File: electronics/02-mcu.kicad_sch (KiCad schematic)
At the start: 30 parts, among them J201 TC2050-IDC-NL, U201 STM32H723VGT6, Y201 25 MHz / 10 ppm

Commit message: Passe le microcontrôleur en LQFP144 et lit les deux courants au même instant
Le LQFP100 avait ses seize entrées ADC prises — douze voies de ligne, trois
de télémétrie, une sortie de multiplexeur — et c'est ce multiplexeur qui
posait le vrai problème : il interdisait par construction de lire les deux
courants moteur ensemble. On lisait un moteur, on commutait, on attendait
l'établissement, on lisait l'autre. Le STM32H723ZGT6 en LQFP144 place
PF11 sur ADC1_INP2 et PF13 sur ADC2_INP2 : même numéro de voie sur deux
convertisseurs, donc une lecture simultanée en mode double, et le 74HC4051
disparaît de la carte.

Le brochage étant donné par nom de port et non par numéro de broche, le
passage a coûté deux affectations sur quatre-vingt-sept. Une affectation est
un choix de port — PA0 porte la voie de ligne 00 — jamais un choix de patte.
Une table numérotée aurait demandé de recopier 144 lignes à la main, et une
erreur de brochage ne se voit pas à l'ERC.

Ajoute une huitième feuille, les témoins de ligne. Ce qu'on regarde pendant
un essai n'est pas un témoin d'état générique, c'est ce que voit la
moustache : une LED par capteur, à l'aplomb du capteur qu'elle rapporte, et
un capteur borgne se voit avant la course plutôt qu'après. Le rapport
cyclique suit le signal, sinon rien ne dirait si la ligne est au bord ou au
centre du trait. PCA9685 à l'adresse 0x40 sur I²C2, 52 octets par rafale
soit 1,2 ms à 400 kHz, en DMA hors de la boucle rapide.

Remplace l'interrupteur à glissière par une mise sous tension à bouton
poussoir : une impulsion amorce, le microcontrôleur se tient lui-même, et
c'est lui qui coupe. La glissière demandait une place au bord de carte que
le pack, l'équilibrage et les fils de l'ESC ont fini par prendre — et elle
ne savait pas éteindre proprement, couper le 3,3 V sous les pieds du
firmware n'ayant jamais rien écrit dans la flash.

Ajoute au générateur le contrôle qui manquait : deux extrémités de nets
différents au même point. Il a fallu qu'il relie B+ à B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
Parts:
- removed TP201: BOOT0, TestPoint:TestPoint_Pad_D1.5mm, symbol Connector:TestPoint
- removed TP202: TP_PE4, TestPoint:TestPoint_Pad_D1.5mm, symbol Connector:TestPoint
- removed TP203: TP_PE5, TestPoint:TestPoint_Pad_D1.5mm, symbol Connector:TestPoint
- removed TP204: TP_PA15, TestPoint:TestPoint_Pad_D1.5mm, symbol Connector:TestPoint
- removed TP205: TP_PC13, TestPoint:TestPoint_Pad_D1.5mm, symbol Connector:TestPoint
- removed TP206: TP_PC14, TestPoint:TestPoint_Pad_D1.5mm, symbol Connector:TestPoint
- removed TP207: TP_PC15, TestPoint:TestPoint_Pad_D1.5mm, symbol Connector:TestPoint
- added C217, C218, C219, C220, C221, C222: 100nF, Capacitor_SMD:C_0402_1005Metric, symbol Device:C
- added SW603: RESET, Button_Switch_SMD:SW_SPST_B3U-1000P, symbol Switch:SW_Push
- C201, C202, C203, C204, C205, C207, C208, C210, C214: footprint Capacitor_SMD:C_0603_1608Metric -> Capacitor_SMD:C_0402_1005Metric; Dielectric (none) -> X7R; Voltage (none) -> 25V
- C206: value 4u7F/10V -> 4u7F; Dielectric (none) -> X5R; Voltage (none) -> 10V
- C209, C211: footprint Capacitor_SMD:C_0603_1608Metric -> Capacitor_SMD:C_0402_1005Metric; Dielectric (none) -> X5R; Voltage (none) -> 16V
- C212, C213: value 2u2F/10V -> 2u2F; Dielectric (none) -> X5R; Voltage (none) -> 10V
- C215, C216: footprint Capacitor_SMD:C_0603_1608Metric -> Capacitor_SMD:C_0402_1005Metric; Dielectric (none) -> C0G; Voltage (none) -> 50V
- J201: value TC2050-IDC-NL -> TC2030-IDC-FP; footprint Connector:Tag-Connect_TC2050-IDC-NL_2x05_P1.27mm_Vertical -> Connector:Tag-Connect_TC2030-IDC-FP_2x03_P1.27mm_Vertical; symbol Connector:TC2050 -> Connector:TC2030
- R201, R202, R203, R204: footprint Resistor_SMD:R_0603_1608Metric -> Resistor_SMD:R_0402_1005Metric; Power (none) -> 63mW
- U201: value STM32H723VGT6 -> STM32H723ZGT6; footprint Package_QFP:LQFP-100_14x14mm_P0.5mm -> Package_QFP:LQFP-144_20x20mm_P0.5mm; symbol MCU_ST_STM32H7:STM32H723VGTx -> MCU_ST_STM32H7:STM32H723ZGTx; LCSC C730142 -> C730146
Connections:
- net IR_LASER_EN is gone; now on net LINE_02: U201.36 (PA2)
- net LED_ERROR is gone; now on net SW_DOWN: U201.65 (PE12)
- net LED_STATUS is gone; now on net +3V3: U201.62 (VDD)
- net LED_USER is gone; now on net MOT_R_IN1: U201.66 (PE13)
- net TOF_F_INT is gone; now on net ENC_R_B: U201.97 (PC7)
- net TP_PE4 is gone; now on net CHG_INT: U201.3 (PE4)
- net +3V3: now also U201.108 (VDD), U201.121 (VDD), U201.131 (VDD), U201.143 (PDR_ON), U201.144 (VDD), U201.17 (VDD), U201.30 (VDD), U201.39 (VDD), U201.52 (VDD), U201.72 (VDD), U201.84 (VDD), U201.95 (VDD33USB), C217.1, C218.1, C219.1, C220.1, C221.1, C222.1; no longer U201.100 (VDD), U201.11 (VDD), U201.27 (VDD), U201.50 (VDD), U201.75 (VDD)
- net +3V3A: now also U201.32 (VREF+), U201.33 (VDDA); no longer U201.20 (VREF+), U201.21 (VDDA)
- net BLE_PWR_EN: now also U201.100 (PA8); no longer U201.67 (PA8)
- net BLE_RX: now also U201.102 (PA10); no longer U201.69 (PA10)
- net BLE_TX: now also U201.101 (PA9); no longer U201.68 (PA9)
- net BOOT0: now also U201.138 (BOOT0); no longer U201.94 (BOOT0)
- net BUZZER: now also U201.140 (PB9); no longer U201.96 (PB9)
- net CHG_CD_EN: now also U201.2 (PE3); no longer U201.1 (PE2)
- net CHG_INT: no longer U201.2 (PE3)
- net ENC_L_A: now also U201.134 (PB4(NJTRST)); no longer U201.90 (PB4(NJTRST))
- net ENC_L_B: now also U201.135 (PB5); no longer U201.91 (PB5)
- net ENC_R_A: now also U201.96 (PC6); no longer U201.63 (PC6)
- net ENC_R_B: no longer U201.64 (PC7)
- net ESC_PWM: now also U201.139 (PB8); no longer U201.95 (PB8)
- net FLASH_MISO: now also U201.112 (PC11); no longer U201.79 (PC11)
- net FLASH_MOSI: now also U201.113 (PC12); no longer U201.80 (PC12)
- net FLASH_SCK: now also U201.111 (PC10); no longer U201.78 (PC10)
- net FLASH_nCS: now also U201.116 (PD2); no longer U201.83 (PD2)
- net GND: now also J201.6, U201.107 (VSS), U201.120 (VSS), U201.130 (VSS), U201.16 (VSS), U201.31 (VSSA), U201.38 (VSS), U201.51 (VSS), U201.61 (VSS), U201.83 (VSS), U201.94 (VSS), C217.2, C218.2, C219.2, C220.2, C221.2, C222.2, SW603.2; no longer J201.3, J201.5, J201.9, U201.10 (VSS), U201.19 (VSSA), U201.26 (VSS), U201.49 (VSS), U201.74 (VSS), U201.99 (VSS)
- net IMU_MISO: now also U201.75 (PB14); no longer U201.53 (PB14)
- net IMU_MOSI: now also U201.76 (PB15); no longer U201.54 (PB15)
- net IMU_SCK: now also U201.74 (PB13); no longer U201.52 (PB13)
- net IMU_nCS: now also U201.73 (PB12); no longer U201.51 (PB12)
- net IPROPI_L: now also U201.49 (PF11); no longer U201.16 (PC1)
- net IPROPI_R: now also U201.53 (PF13); no longer U201.17 (PC2_C)
- net IR_BANK_A: now also U201.58 (PE7); no longer U201.37 (PE7)
- net IR_BANK_B: now also U201.59 (PE8); no longer U201.38 (PE8)
- net LINE_00: now also U201.34 (PA0); no longer U201.22 (PA0)
- net LINE_01: now also U201.35 (PA1); no longer U201.23 (PA1)
- net LINE_02: no longer U201.24 (PA2)
- net LINE_03: now also U201.37 (PA3); no longer U201.25 (PA3)
- net LINE_04: now also U201.40 (PA4); no longer U201.28 (PA4)
- net LINE_05: now also U201.41 (PA5); no longer U201.29 (PA5)
- net LINE_06: now also U201.42 (PA6); no longer U201.30 (PA6)
- net LINE_07: now also U201.43 (PA7); no longer U201.31 (PA7)
- net LINE_08: now also U201.46 (PB0); no longer U201.34 (PB0)
- net LINE_09: now also U201.47 (PB1); no longer U201.35 (PB1)
- net LINE_10: now also U201.44 (PC4); no longer U201.32 (PC4)
- net LINE_11: now also U201.45 (PC5); no longer U201.33 (PC5)
- net MOT_L_IN1: now also U201.60 (PE9); no longer U201.39 (PE9)
- net MOT_L_IN2: now also U201.64 (PE11); no longer U201.41 (PE11)
- net MOT_L_nFAULT: now also U201.117 (PD3); no longer U201.84 (PD3)
- net MOT_L_nSLEEP: now also U201.114 (PD0); no longer U201.81 (PD0)
- net MOT_R_IN1: no longer U201.43 (PE13)
- net MOT_R_IN2: now also U201.67 (PE14); no longer U201.44 (PE14)
- net MOT_R_nFAULT: now also U201.118 (PD4); no longer U201.85 (PD4)
- net MOT_R_nSLEEP: now also U201.115 (PD1); no longer U201.82 (PD1)
- net NRST: now also J201.3, U201.25 (NRST), SW603.1; no longer J201.10, U201.14 (NRST)
- net OSC_IN: now also U201.23 (PH0); no longer U201.12 (PH0)
- net OSC_OUT: now also U201.24 (PH1); no longer U201.13 (PH1)
- net SCL2: now also U201.69 (PB10); no longer U201.46 (PB10)
- net SDA2: now also U201.70 (PB11); no longer U201.47 (PB11)
- net START_BTN: now also U201.85 (PD14); no longer U201.61 (PD14)
- net SWCLK: now also U201.109 (PA14(JTCK); no longer U201.76 (PA14(JTCK)
- net SWDIO: now also J201.5, U201.105 (PA13(JTMS); no longer J201.2, U201.72 (PA13(JTMS)
- net SWO: now also J201.2, U201.133 (PB3(JTDO); no longer J201.6, U201.89 (PB3(JTDO)
- net SW_DOWN: no longer U201.42 (PE12)
- net SW_LEFT: now also U201.68 (PE15); no longer U201.45 (PE15)
- net SW_PUSH: now also U201.82 (PD13); no longer U201.60 (PD13)
- net SW_RIGHT: now also U201.79 (PD10); no longer U201.57 (PD10)
- net SW_UP: now also U201.63 (PE10); no longer U201.40 (PE10)
- net USB_DM: now also U201.103 (PA11); no longer U201.70 (PA11)
- net USB_DP: now also U201.104 (PA12); no longer U201.71 (PA12)
- net VBAT_SENSE: now also U201.26 (PC0); no longer U201.15 (PC0)
- net VCAP1: now also U201.71 (VCAP); no longer U201.48 (VCAP)
- net VCAP2: now also U201.106 (VCAP); no longer U201.73 (VCAP)
- net SCL1: no longer names the net of U201.92 (PG7)
- net SDA1: no longer names the net of U201.93 (PG8)
- net TOF_ANA: no longer names the net of U201.18 (PF6)
- net TOF_FL_INT: no longer names the net of U201.98 (PC8)
- net TOF_FL_XSHUT: no longer names the net of U201.87 (PG2)
- net TOF_F_XSHUT: no longer names the net of U201.86 (PD15)
- net TP_PA15: no longer names the net of U201.77 (PD8)
- net TP_PC13 renamed TX_L
- net TP_PC14: no longer names the net of U201.8 (PC14)
- net TP_PC15: no longer names the net of U201.9 (PC15)
- net TP_PE5 renamed TRACK_EN
- new net PWR_BTN: U201.142 (PE1)
- new net PWR_HOLD: U201.141 (PE0)
- new net RX_F: U201.27 (PC1)
- new net RX_FL: U201.28 (PC2_C)
- new net RX_L: U201.29 (PC3_C)
- new net TX_F: U201.48 (PB2)
- new net TX_FL: U201.1 (PE2)
- no-connect marks 7 -> 45
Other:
- note added: "Bilan : 80 broches affectees, 45 libres et marquees non connectees au schema. Le LQFP144 apporte les ports F et G, soit 32 E/S de plus et surtout DOUZE entrees ADC supplementaires (PF3 a PF14) : c est ce qui a permis de supprimer le multiplexeur 74HC4051 et de lire les deux courants moteur au meme instant."
- note added: "C208/C209 : VDDA. C210/C211 : VREF+. C222 : VDD33USB, broche separee sur le LQFP144 alors que le LQFP100 la reliait en interne. VCAP : 2,2 uF ceramique, ESR < 2 ohm, tres pres du boitier. PDR_ON est tiree a VDD : reset interne d alimentation actif."
- note added: "Debogage SWD + SWO - Tag-Connect TC2030 (brochage Sp3ctra V4)"
- note added: "Decouplage - un 100 nF par broche VDD (elles sont onze)"
- note added: "Rails analogiques, USB et VCAP"
- note removed: "Bilan : 74 broches affectees sur 82 disponibles."
- note removed: "C208/C209 : VDDA C210/C211 : VREF+"
- note removed: "Debogage SWD + SWO - Tag-Connect TC2050-IDC-NL"
- note removed: "Decouplage - un 100 nF par broche VDD, au plus pres du boitier"
- note removed: "PD7-PD9 et PD11-PD12 restent libres, marques non connectes au schema."
- note removed: "Reserves sorties sur pastilles"
- note removed: "VCAP : 2,2 uF ceramique, ESR < 2 ohm, tres pres du boitier."
- title: UsainBot - STM32H723VGT6, horloge et debogage -> UsainBot - STM32H723ZGT6, horloge et debogage
- moved on the sheet: C201, C202, C203, C204, C205, C206, C207, C208, C209, C210, C211, C212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
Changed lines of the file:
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@@
 	(paper "A3")
 	(title_block
-		(title "UsainBot - STM32H723VGT6, horloge et debogage")
+		(title "UsainBot - STM32H723ZGT6, horloge et debogage")
 		(date "2026-08-30")
 		(rev "A")
 		(company "Pacabot")
-		(comment 1 "Mode LDO seul (AN5312) : le LQFP100 n expose pas les broches SMPS")
-		(comment 2 "PB3 est reserve au SWO, d ou l abandon de TIM2")
+		(comment 1 "Mode LDO seul (AN5312) : le LQFP144 n expose pas les broches SMPS")
+		(comment 2 "Passe du LQFP100 au LQFP144 le 4 septembre : 12 entrees ADC de plus")
 	)

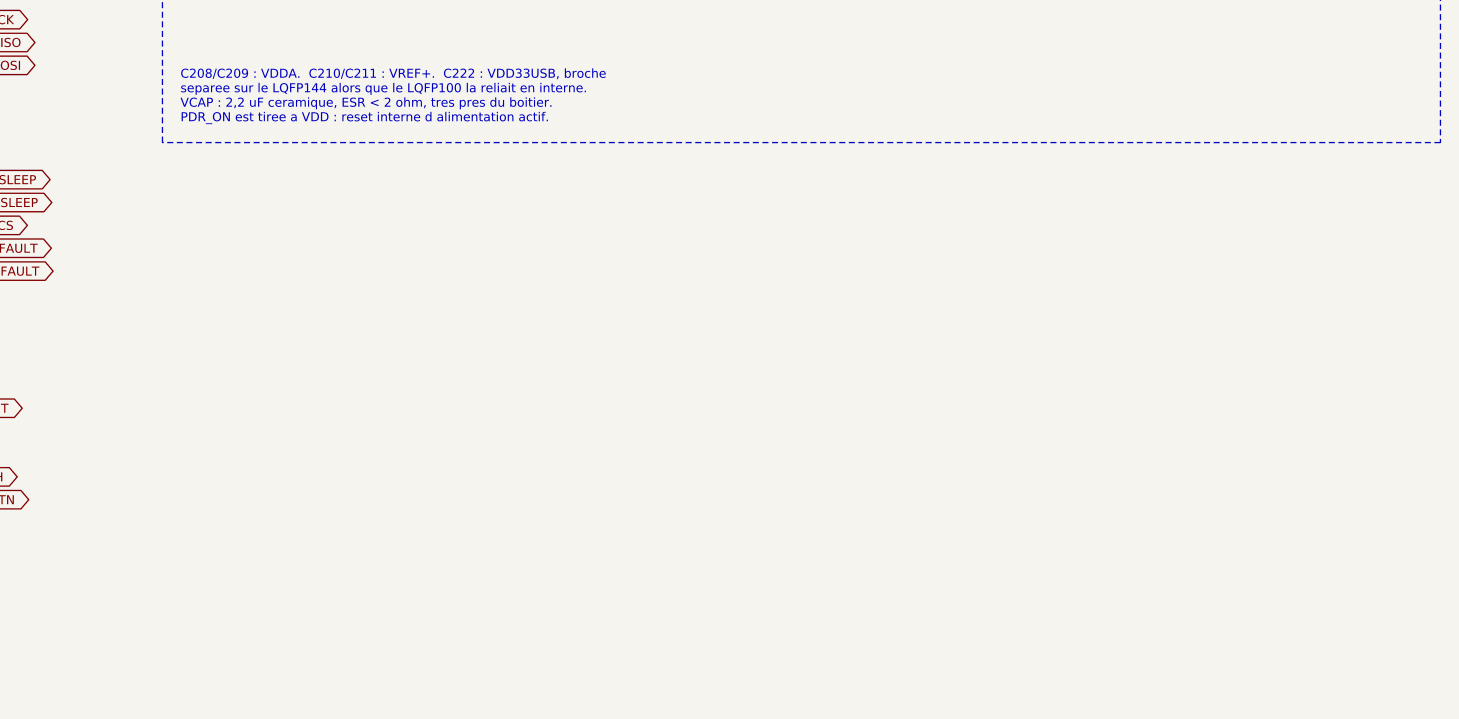
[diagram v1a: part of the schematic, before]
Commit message: Replace la carte autour de ses chaînes analogiques et y intègre le pack commun et l'ESC
Le placement du 4 septembre rangeait les pièces par zone. Celui-ci part des
nets et des vraies pastilles, et affecte chaque condensateur à une broche
plutôt qu'à une couronne autour du boîtier. Le STM32 pivote de 180° sur son
centre pour tourner son côté analogique vers la barrette. Chaque station
laser reçoit son propre TLV9064 (U504 s'ajoute pour la station L), et la
liaison photodiode → TIA tombe de 34, 56 et 69 mm à 3,1, 7,4 et 2,9 mm. La
boucle de retour du TIA passe de 140–150 mm à 3,55. Cinq découplages
suivent : C568, C569/C570 sur VREF_RX, C223/C224 sur VBAT du MCU et C351
sur VREF_MOT du pont droit.

`layout.py`, `layout_fit.json` et `place_pcb.py --reset` ne décrivent plus
cette carte. Le README le dit en tête, et les nouveaux outils partent du
PCB courant, jamais de l'ancienne table. `audit_placement_geometry.py` relit
les courtyards orientés et les contrôle sous Shapely, `placement_metrics.py`
et `preview_analog_paths.py` mesurent distances et couloirs sans poser une
piste. `refine_placement.py` calcule la table, `apply_refined_placement.py`
l'écrit en vérifiant verrous et UUID : il ne se rejoue pas après une
retouche à la main.

L'alimentation change de nature. Le pack LiFePO4 et son ESC sur VBAT
laissent place à un pack 2S commun, chimie encore à choisir, que la carte,
les moteurs et la turbine partagent. Une seule prise MR30 à trois contacts
porte GND, point milieu et VPACK, et remplace XT30 + JST-XH. L'ESC devient
un EMAX Bullet 12A (12 A continu, 15 A crête, sans BEC) sur VPACK brut,
monté debout sur J103. J104 et J702 disparaissent. ESC103 et M703 sont des
symboles hors carte : les phases moteur ne reçoivent aucun pad fictif, et
le module ne compte qu'une fois dans la nomenclature. R107 passe de 10 à
47 Ω pour ramener l'équilibrage à 88 mA et 0,36 W, sous le watt de son
boîtier 2512. La recharge reste inhibée par défaut matériel tant que
cellules, profil et fir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
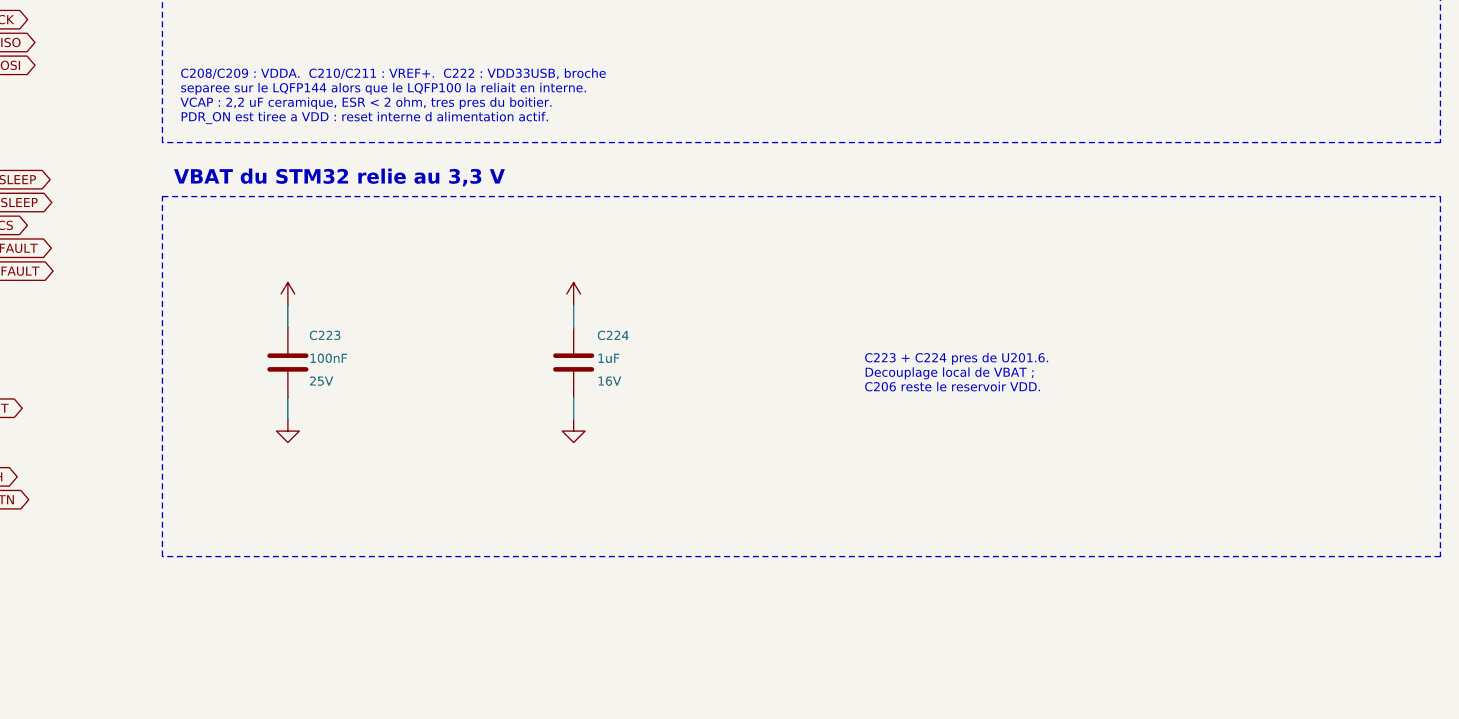
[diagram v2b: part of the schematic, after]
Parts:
- added C223: 100nF, Capacitor_SMD:C_0402_1005Metric, symbol Device:C
- added C224: 1uF, Capacitor_SMD:C_0402_1005Metric, symbol Device:C
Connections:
- net +3V3: now also C223.1, C224.1
- net GND: now also C223.2, C224.2
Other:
- note added: "C223 + C224 pres de U201.6. Decouplage local de VBAT ; C206 reste le reservoir VDD."
- note added: "VBAT du STM32 relie au 3,3 V"

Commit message: Alimente les codeurs en 5 V, renomme les paires USB et passe les résistances des LED en 0603
- Codeurs IE2 : U302 TPS70950 sur VBAT (EN sur +3V3, le 5 V suit le MCU
  dont les entrées FT_h ne tolèrent 5 V qu'alimentées), C310 1 µF et
  C311 4,7 µF ; net /Moteurs/ENC_5V vers J301.4 et J351.4, classe
  ALIM_LOGIQUE. Symbole Pacabot:TPS70950DBV ajouté à la bibliothèque.
- Paires USB : USB_D_P/N et /Alimentation/USB_C_D_P/N, reconnues comme
  paires par KiCad et par le routeur de paires du fork.
- R615, R617, R618 en 0603 à 390/560/560 ohms (≈ 10 mA, ≤ 50 mW à 7,3 V) ;
  R615 et R618 recalées, D609 décalée de 0,25 mm, R617 déplacée à côté
  de R306 faute de place pour une 0603 près de D608.

Schéma et carte concordent pastille par pastille (netlist KiCad 10.0.1) ;
ERC 0, DRC sans nouvelle violation. Détail dans rules-review/README.md.

Co-Authored-By: Claude Opus 5.5 <noreply@anthropic.com>
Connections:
- net USB_DM renamed USB_D_N
- net USB_DP renamed USB_D_P
